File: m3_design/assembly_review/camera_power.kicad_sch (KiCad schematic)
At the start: 22 parts, among them U7 TPS259570DSGR, U8 AP63301WU-7

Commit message: R10: m3_design/r10_build.sh and per-family stage gate; m3_design/assembly_review rebuilt as M3-ASSY-R10 (board 883d2db5..., 46 x 90 mm); tools/check.sh passes at zero; binding note bound to the board
Co-Authored-By: Claude Opus 5.5 <noreply@anthropic.com>
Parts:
- removed C70: 4.7nF 50V C0G 5%, rocket:C_0603_1608Metric, symbol M3:C
- removed C71, C74: 100nF 50V X7R 10%, rocket:C_0603_1608Metric, symbol M3:C
- removed C72, C73, C75, C76: 22uF 25V X7R 10%, rocket:M3_GRM32_1210, symbol M3:C
- removed C77: 47pF 50V C0G 5%, rocket:C_0603_1608Metric, symbol M3:C
- removed L3: 6.8uH, rocket:M3_SRP5030TA, symbol M3:L
- removed R70: 1.78k 0.1%, rocket:R_0603_1608Metric, symbol M3:R
- removed R71: 172k 0.1%, rocket:R_0603_1608Metric, symbol M3:R
- removed R72: 30.9k 0.1%, rocket:R_0603_1608Metric, symbol M3:R
- removed R74, R77: 1k 1%, rocket:R_0603_1608Metric, symbol M3:R
- removed R75, R76, R78: 10k 1%, rocket:R_0603_1608Metric, symbol M3:R
- removed TP70: RAW_PROTECTED, rocket:M3_TestPad_1.5, symbol M3:TestPoint
- removed TP71: CAM_INPUT_LIMITED, rocket:M3_TestPad_1.5, symbol M3:TestPoint
- removed TP73: CAM_ILIM, rocket:M3_TestPad_1.5, symbol M3:TestPoint
- removed U7: TPS259570DSGR, rocket:M3_TPS2595_DSG, symbol M3:CameraEFuse
- removed U8: AP63301WU-7, rocket:M3_AP63200_TSOT26, symbol M3:CameraBuck
- added C400, C401, C403, C404, C405, C406, C407, C411, C421, C431: 22uF 25V X7R 10%, rocket:M3_GRM32_1210, symbol M3:C
- added C402, C410, C420, C430: 100nF 50V X7R 10%, rocket:C_0603_1608Metric, symbol M3:C
- added C408: 10nF 50V X7R 10%, rocket:C0402, symbol M3:C
- added L400: 6.8uH, rocket:M3_SRP5030TA, symbol M3:L
- added R400: 56.2k 0.1%, rocket:R_0603_1608Metric, symbol M3:R
- added R401, R403, R412, R422, R432: 10k 0.1%, rocket:R_0603_1608Metric, symbol M3:R
- added R402: 49.9k 0.1%, rocket:R_0603_1608Metric, symbol M3:R
- added R404: 2k 1%, rocket:R_0603_1608Metric, symbol M3:R
- added R405: 820R 1%, rocket:R_0603_1608Metric, symbol M3:R
- added R410, R411, R421, R431: 100k 1%, rocket:R_0603_1608Metric, symbol M3:R
- added R420: 66.5k 1%, rocket:R_0603_1608Metric, symbol M3:R
- added R430: 22.6k 1%, rocket:R_0603_1608Metric, symbol M3:R
- added U400: AP63201WU-7, rocket:M3_AP63200_TSOT26, symbol M3:CameraBuck
- added U401: TPS7A9101DSKR, rocket:M3_TPS7A91_DSK10, symbol M3:PortLDO
- added U402, U410, U420: TPS2553DBVR, rocket:M3_TPS2553_DBV, symbol M3:USBCurrentLimit
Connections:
- net 3V3: now also R412.2, R422.2, R432.2
- net CAM_5V: now also C431.1, U402.6 (OUT)
- net CAM_FAULT_N: now also R432.1, U402.4 (FAULT_N)
- net CAM_ILIM: now also R430.1, U402.5 (ILIM)
- net CAM_PWR_EN: now also R431.1, U402.3 (EN)
- net GND: now also C400.2, C401.2, C403.2, C404.2, C405.2, C406.2, C407.2, C408.2, C410.2, C411.2, C420.2, C421.2, C430.2, C431.2, R401.2, R403.2, R405.2, R410.2, R411.2, R420.2, R421.2, R430.2, R431.2, U400.4 (GND), U401.11 (PAD), U401.4 (GND), U401.6 (SS_CTRL), U402.2 (GND), U410.2 (GND), U420.2 (GND)
- net RAW_PROTECTED: now also C400.1, C401.1, U400.2 (EN), U400.3 (IN)
- new net GPS_4V8: C411.1, U410.6 (OUT)
- new net GPS_FAULT_N: R412.1, U410.4 (FAULT_N)
- new net GPS_ILIM: R410.1, U410.5 (ILIM)
- new net GPS_PWR_EN: R411.1, U410.3 (EN)
- new net PORT_4V8: C406.1, C407.1, C410.1, C420.1, R402.1, R405.1, U401.1 (OUT), U401.2 (OUT), U410.1 (IN), U420.1 (IN)
- new net PORT_5V3: C403.1, C404.1, C405.1, C430.1, L400.2, R400.1, U401.10 (IN), U401.7 (EN), U401.9 (IN), U402.1 (IN)
- new net PORT_BST: C402.1, U400.6 (BST)
- new net PORT_FB: R401.1, R404.2, U400.1 (FB)
- new net PORT_FB_TOP: R400.2, R404.1
- new net PORT_LDO_FB: R402.2, R403.1, U401.3 (FB)
- new net PORT_LDO_SS: C408.1, U401.8 (NR_SS)
- new net PORT_SW: C402.2, L400.1, U400.5 (SW)
- new net RADIO_4V8: C421.1, U420.6 (OUT)
- new net RADIO_FAULT_N: R422.1, U420.4 (FAULT_N)
- new net RADIO_ILIM: R420.1, U420.5 (ILIM)
- new net RADIO_PWR_EN: R421.1, U420.3 (EN)
- no-connect marks 0 -> 1
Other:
- note added: "All three TPS2553 enables have 100k pull-downs; fault pull-ups use main 3V3 only. R405 sets the LDO minimum load."
- note added: "Firmware: disable UART OE before port power; hold all EN/OE low throughout reset, boot and load shedding. FAULT delay is not battery-drop detection."
- note added: "R10 O5: RAW_PROTECTED -> AP63201 5.456V -> camera limiter; TPS7A91 4.792V -> separate GPS and radio limiters."
- note added: "Switch current limits and endpoint-voltage budgets: sources/r10_design/parts_qualification.md. Bench transient/inrush verification remains required."
- note removed: "05 | Camera branch protection and regulator"
- note removed: "5 V camera class: 5.253 V nominal at output caps; 1 A target, bench qualification pending."
- note removed: "CAM_PWR_EN LOW/reset = OFF. FLT_N reports protection, not power-good."
- note removed: "RAW_PROTECTED: supplied by U9 battery protection; not connected to USB."
- company: Single-board M3 candidate; full system incomplete -> (none)
- title: 05 | Camera branch protection and regulator -> 05 | Regulated camera, radio and GPS port supplies

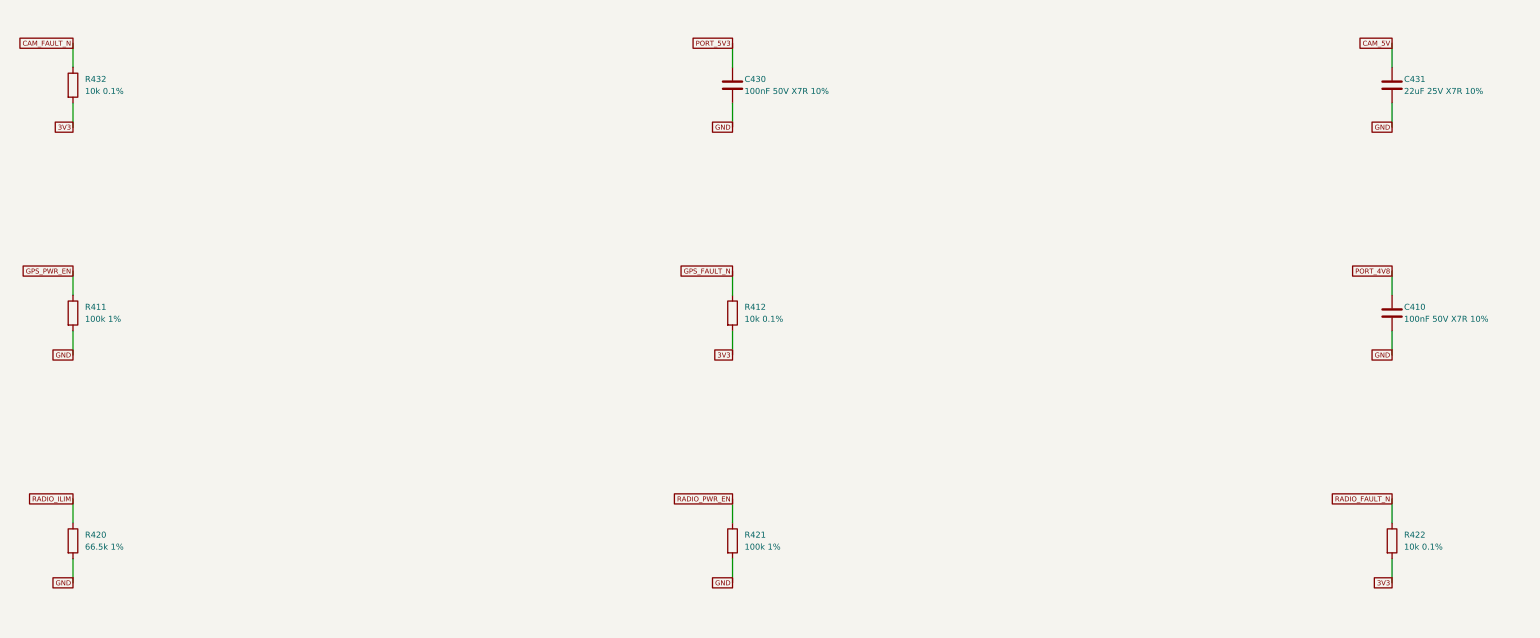
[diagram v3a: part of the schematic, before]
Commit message: R10 requirements-audit cuts and GAP fixes before review round 9
Implement adopted AUD-1 through AUD-10 and GAP-1 through GAP-5 after the single-switch pass.
Remove the advisory pull-pin, redundant probes and GPS/radio IO LDO cells; qualify the smaller
AONR21357 pair, correct C120 voltage rating, standardize shared-code capacitor lands, simplify
slow returns and fire-only copper, localize U9 output protection and add exactly two U401 VIPPO vias.
Record physical-current timing, coupled fire/source budget, C84 manual fitting and narrowed gate scopes.

Board SHA-256: 877d01996a59e9dd5c6dbc367274bb9a323a13982d67960fe46df9b0ee53205d
Board: 46 x 90 mm, 4 layers, 2365477 bytes; 225 footprints, 883 straight tracks, 323 vias.
Netlist SHA-256: 0843da709e2d7a757e9b35cdff48158a54012c5353619cbf409ab961efd2c3ca
Two fresh complete passing builds are byte-identical. Schematic: 700 pins; 22 seeded faults detected.

Final unskipped tools/check.sh: exit 0
DRC violations 0  unconnected 0  schematic parity 0  ERC 0
metadata / 3D model audit: OK
silkscreen outside the board outline: 0 stroke points
fit check: OK (CAD envelopes only)
R10 CAD contract (full): OK
routing hygiene: 0 failing, 0 allowlisted, 0 leftovers recorded
actuator safety contract: OK
Fab manifest: OK; 5 outputs match current CAD and export inputs
Self-tests: shell 4, fit 24, paste 5, routing 59, R10 131; three NumPy cases rerun and passed.

Fab: 215 CPL rows, 82 BOM codes; orientation / paste / manifest pass. Hot-plug: 2304 required
cases plus convergence and controls pass (simulation / Inference). Plate f1 280.9 Hz (Inference).
Live JLC: $84.43 vs $84.41 target, 46 Extended codes; R430 / U4 short. Procurement exit 1 is a
disclosed OQ-3 / ordering deviation, not a CAD gate pass. No quote accepted or order placed.
Firmware, bench, thermal/transient correlation, process acceptance, installed RF immunity and physical fit unverified.

This preparatory pass earns no clean-review credit. Start fresh full ten-lens round 9 on th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
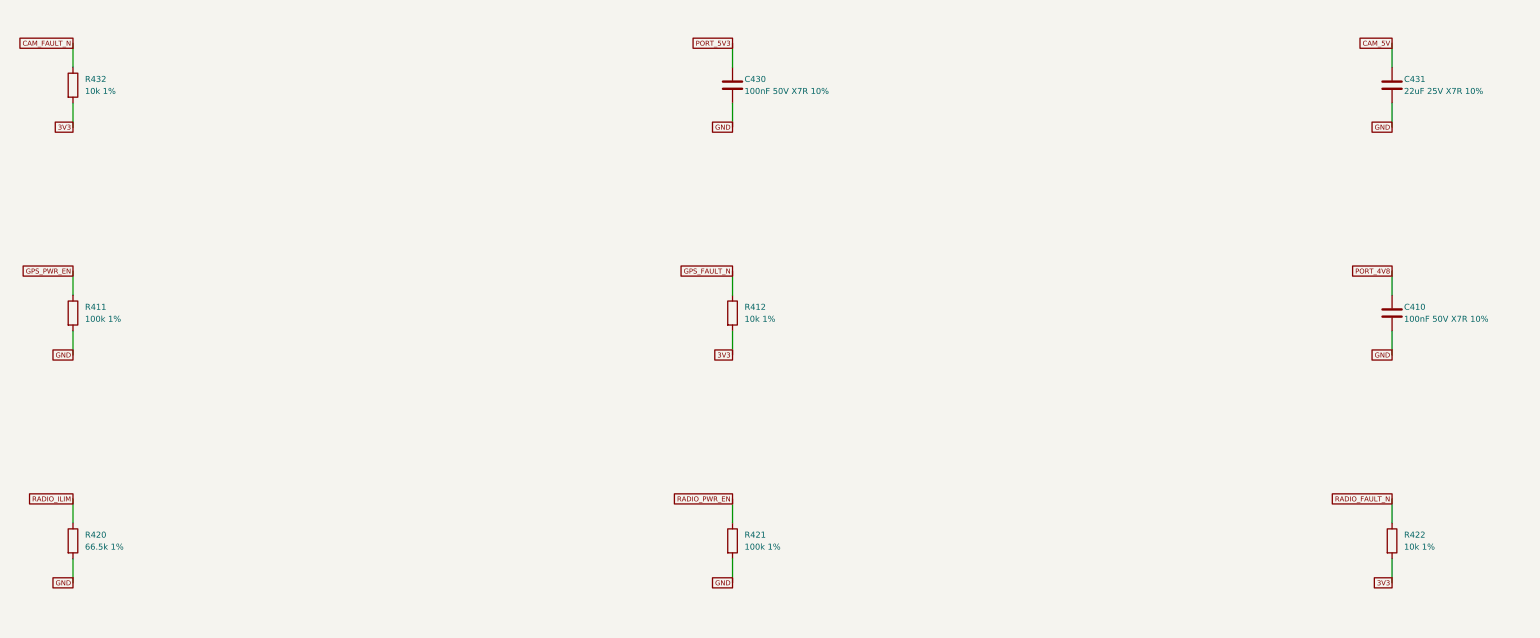
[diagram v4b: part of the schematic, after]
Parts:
- R412, R422, R432: value 10k 0.1% -> 10k 1%; footprint rocket:R_0603_1608Metric -> rocket:R0402; LCSC C95204 -> C25744; Manufacturer YAGEO -> UNI-ROYAL(Uniroyal Elec); Manufacturer Part RT0603BRD0710KL -> 0402WGF1002TCE
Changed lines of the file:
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@@
 					(size 1.27 1.27))
 				(justify left)))
-		(property "Value" "10k 0.1%"
+		(property "Value" "10k 1%"
 			(at 88.9 283.21 0)
 			(effects
@@
 					(size 1.27 1.27))
 				(justify left)))
-		(property "Footprint" "rocket:R_0603_1608Metric"
+		(property "Footprint" "rocket:R0402"
 			(at 86.36 281.94 0)
 			(hide yes)
@@
 					(size 1.27 1.27))
 				(justify left)))
-		(property "Datasheet" "https://www.lcsc.com/product-detail/C95204.html"
+		(property "Datasheet" "https://datasheet.lcsc.com/datasheet/pdf/0a975aaa49b7c97f38a963127be4a823.pdf"
 			(at 86.36 281.94 0)
 			(hide yes)
@@
 					(size 1.27 1.27))
 				(justify left)))
-		(property "LCSC" "C95204"
+		(property "LCSC" "C25744"
 			(at 86.36 281.94 0)
 			(hide yes)
@@
 					(size 1.27 1.27))
 				(justify left)))
-		(property "Manufacturer" "YAGEO"
+		(property "Manufacturer" "UNI-ROYAL(Uniroyal Elec)"
 			(at 86.36 281.94 0)
 			(hide yes)
@@
 					(size 1.27 1.27))
 				(justify left)))
-		(property "Manufacturer Part" "RT0603BRD0710KL"
+		(property "Manufacturer Part" "0402WGF1002TCE"
 			(at 86.36 281.94 0)
 			(hide yes)
@@
 					(size 1.27 1.27))
 				(justify left)))
-		(property "Value" "10k 0.1%"
+		(property "Value" "10k 1%"
 			(at 228.6 331.47 0)
 			(effects
@@
 					(size 1.27 1.27))
 				(justify left)))
-		(property "Footprint" "rocket:R_0603_1608Metric"
+		(property "Footprint" "rocket:R0402"
 			(at 226.06 330.2 0)
 			(hide yes)
@@
 					(size 1.27 1.27))
 				(justify left)))
-		(property "Datasheet" "https://www.lcsc.com/product-detail/C95204.html"
+		(property "Datasheet" "https://datasheet.lcsc.com/datasheet/pdf/0a975aaa49b7c97f38a963127be4a823.pdf"
 			(at 226.06 330.2 0)
 			(hide yes)
@@
 					(size 1.27 1.27))
 				(justify left)))
-		(property "LCSC" "C95204"
+		(property "LCSC" "C25744"
 			(at 226.06 330.2 0)
 			(hide yes)
@@
 					(size 1.27 1.27))
 				(justify left)))
-		(property "Manufacturer" "YAGEO"
+		(property "Manufacturer" "UNI-ROYAL(Uniroyal Elec)"
 			(at 226.06 330.2 0)
 			(hide yes)
@@
 					(size 1.27 1.27))
 				(justify left)))
-		(property "Manufacturer Part" "RT0603BRD0710KL"
+		(property "Manufacturer Part" "0402WGF1002TCE"
 			(at 226.06 330.2 0)
 			(hide yes)
@@
 					(size 1.27 1.27))
 				(justify left)))
-		(property "Value" "10k 0.1%"
+		(property "Value" "10k 1%"
 			(at 368.3 379.73 0)
 			(effects
@@
 					(size 1.27 1.27))
 				(justify left)))
-		(property "Footprint" "rocket:R_0603_1608Metric"
+		(property "Footprint" "rocket:R0402"
 			(at 365.76 378.46 0)
 			(hide yes)
@@
 					(size 1.27 1.27))
 				(justify left)))
-		(property "Datasheet" "https://www.lcsc.com/product-detail/C95204.html"
+		(property "Datasheet" "https://datasheet.lcsc.com/datasheet/pdf/0a975aaa49b7c97f38a963127be4a823.pdf"
 			(at 365.76 378.46 0)
 			(hide yes)
@@
 					(size 1.27 1.27))
 				(justify left)))
-		(property "LCSC" "C95204"
+		(property "LCSC" "C25744"
 			(at 365.76 378.46 0)
 			(hide yes)
@@
 					(size 1.27 1.27))
 				(justify left)))
-		(property "Manufacturer" "YAGEO"
+		(property "Manufacturer" "UNI-ROYAL(Uniroyal Elec)"
 			(at 365.76 378.46 0)
 			(hide yes)
@@
 					(size 1.27 1.27))
 				(justify left)))
-		(property "Manufacturer Part" "RT0603BRD0710KL"
+		(property "Manufacturer Part" "0402WGF1002TCE"
 			(at 365.76 378.46 0)
 			(hide yes)
